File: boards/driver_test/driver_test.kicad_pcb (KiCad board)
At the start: 4 copper layers, 202.2 x 119.9 mm, 212 parts, among them J1 DIN41612_03x32_C, J2 Barrel_Jack_Switch, J3 Conn_01x24, J4 Conn_01x24, Q1 MMBT2222, Q10 MMBT2907, Q11 MMBT2222, Q12 MMBT2222, Q13 MMBT2222, Q14 MMBT2222, Q15 MMBT2222, Q16 MMBT2907, Q17 MMBT2222, Q18 MMBT2222, Q19 MMBT2222, Q2 MMBT2907, Q20 MMBT2222, Q21 MMBT2222, Q22 MMBT2222, Q23 MMBT2222, Q24 MMBT2222, Q25 MMBT2907, Q26 MMBT2222, Q27 MMBT2907, Q3 MMBT2222, Q4 IRF7413, Q5 MMBT2222, Q6 MMBT2907, Q7 MMBT2222, Q8 MMBT2222, Q9 MMBT2222, T1 1:1, T2 1:1, U1 AD1582BRTZ, U2 74LVC245, U3 JTE0624D05, U4 ADP151-3.3, U5 LTC4231-1, U6 74HC4514, U7 74LVC2G04, U8 SN7524

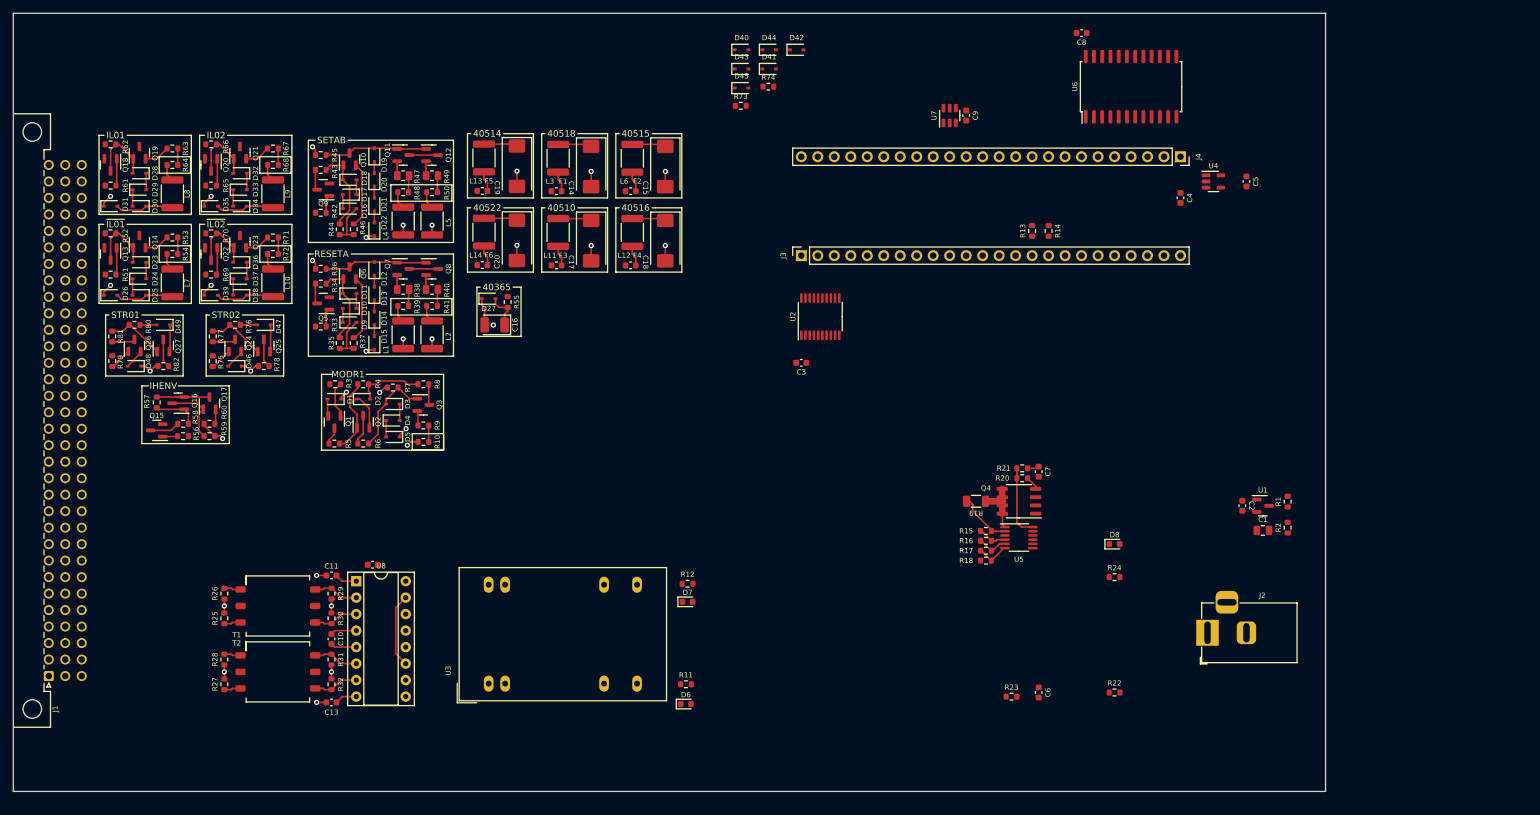
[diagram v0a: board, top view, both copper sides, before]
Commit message: Driver: some high-level board rearrangement and addition of 3d models
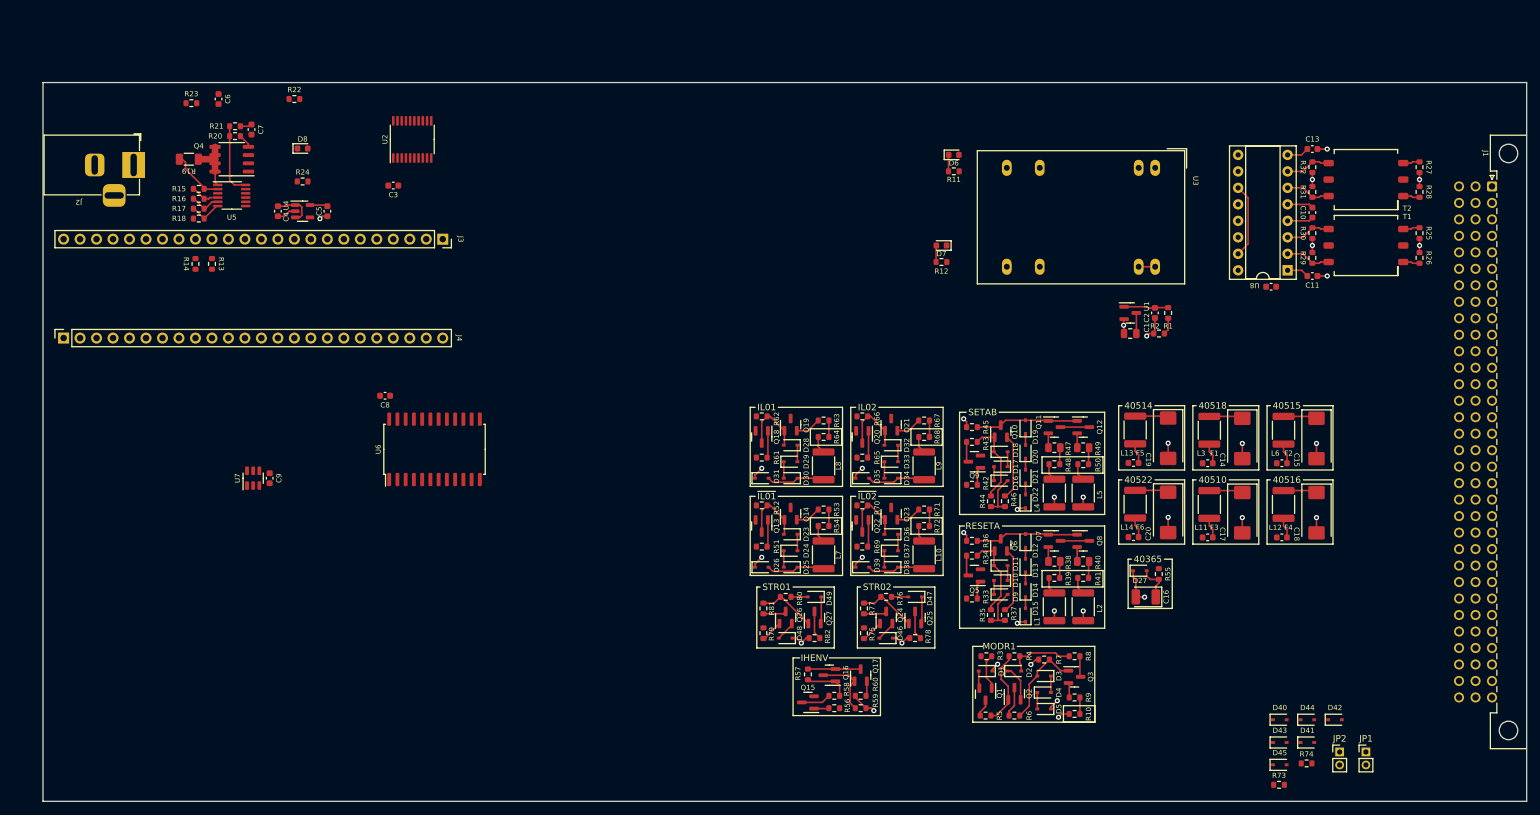
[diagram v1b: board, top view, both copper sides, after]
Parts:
- added JP1: Jumper_2_Open, Connector_PinHeader_2.00mm:PinHeader_1x02_P2.00mm_Vertical, F.Cu at (229.2, 128.5)
- added JP2: Jumper_2_Open, Connector_PinHeader_2.00mm:PinHeader_1x02_P2.00mm_Vertical, F.Cu at (225.2, 128.5)
- moved J1 234.8 mm to (248.7, 41.4), turned to -90 degrees
- moved R27 200.6 mm to (237.5, 38.4), turned to -90 degrees
- moved R28 197.7 mm to (237.5, 42.3), turned to -90 degrees
- moved R25 193.5 mm to (237.5, 48.6), turned to -90 degrees
- moved R26 191.3 mm to (237.5, 52.4), turned to -90 degrees
- moved T2 184.0 mm to (229.2, 40.3), turned to 180 degrees
- moved J2 180.5 mm to (39.4, 38.1), turned to 0 degrees
- moved T1 176.6 mm to (229.2, 50.5), turned to 180 degrees
- moved J4 174.3 mm to (28.6, 64.8), turned to 90 degrees
- moved C13 173.5 mm to (221.0, 35.6), turned to 180 degrees
- moved R32 170.8 mm to (221.0, 38.4), turned to 90 degrees
- moved R31 167.4 mm to (221.0, 42.3), turned to 90 degrees
- moved C10 164.8 mm to (221.0, 45.4), turned to 90 degrees
- moved R30 162.4 mm to (221.0, 48.6), turned to 90 degrees
- moved R29 159.7 mm to (221.0, 52.4), turned to 90 degrees
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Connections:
- net /40311/0V renamed /40311/4036nA
- J1 pad a1: /GAR1 -> unconnected-(J1-Pada1)
- J1 pad a10: /STR2 -> unconnected-(J1-Pada10)
- J1 pad a16: /RFD1 -> unconnected-(J1-Pada16)
- J1 pad a17: /XFN1 -> unconnected-(J1-Pada17)
- J1 pad a18: /RCD1 -> unconnected-(J1-Pada18)
- J1 pad a19: /XCN1 -> unconnected-(J1-Pada19)
- J1 pad a2: /GBR1 -> unconnected-(J1-Pada2)
- J1 pad a20: /RFD2 -> unconnected-(J1-Pada20)
- J1 pad a21: /XFN2 -> unconnected-(J1-Pada21)
- J1 pad a22: /RCD2 -> unconnected-(J1-Pada22)
- J1 pad a23: /XCN2 -> unconnected-(J1-Pada23)
- J1 pad a29: /XRST1 -> unconnected-(J1-Pada29)
- J1 pad a3: /GAR2 -> unconnected-(J1-Pada3)
- J1 pad a30: /RSTRN1 -> unconnected-(J1-Pada30)
- J1 pad a31: /XSET1 -> unconnected-(J1-Pada31)
- J1 pad a32: /SETRN1 -> unconnected-(J1-Pada32)
- J1 pad a4: /GBR2 -> unconnected-(J1-Pada4)
- J1 pad a9: /STR1 -> unconnected-(J1-Pada9)
- J1 pad c1: unconnected-(J1-Padc1) -> /GAR2
- J1 pad c10: unconnected-(J1-Padc10) -> /STR2
- J1 pad c16: unconnected-(J1-Padc16) -> /RFD1
- J1 pad c17: unconnected-(J1-Padc17) -> /XFN1
- J1 pad c18: unconnected-(J1-Padc18) -> /RCD1
- J1 pad c19: unconnected-(J1-Padc19) -> /XCN1
- J1 pad c2: unconnected-(J1-Padc2) -> /GBR2
- J1 pad c20: unconnected-(J1-Padc20) -> /RFD2
- J1 pad c21: unconnected-(J1-Padc21) -> /XFN2
- J1 pad c22: unconnected-(J1-Padc22) -> /RCD2
- J1 pad c23: unconnected-(J1-Padc23) -> /XCN2
- J1 pad c29: unconnected-(J1-Padc29) -> /XRST1
- J1 pad c3: unconnected-(J1-Padc3) -> /GAR1
- J1 pad c30: unconnected-(J1-Padc30) -> /RSTRN1
- J1 pad c31: unconnected-(J1-Padc31) -> /XSET1
- J1 pad c32: unconnected-(J1-Padc32) -> /SETRN1
- J1 pad c4: unconnected-(J1-Padc4) -> /GBR1
- J1 pad c9: unconnected-(J1-Padc9) -> /STR1
- R73 pad 1: /XRST1 -> Net-(JP1-Pad2)
- R74 pad 1: /XSET1 -> Net-(JP2-Pad2)
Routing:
- net GND: track 67.3 -> 77.6 mm, vias 30 -> 33
- net Net-(C2-Pad1): track 0.00 -> 6.88 mm
- net Net-(C4-Pad2): track 0.00 -> 6.30 mm
- net +5V: track 0.00 -> 3.18 mm
- net +3V3: track 0.00 -> 2.74 mm
- net /VREF: track 4.02 -> 6.61 mm
- net Net-(D7-Pad2): track 0.00 -> 2.56 mm
- net Net-(D6-Pad1): track 0.00 -> 2.56 mm
- net Net-(J2-Pad1): track 8.53 -> 11.1 mm
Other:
- board size 202.2 x 119.9 mm -> 228.6 x 110.7 mm

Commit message: Driver test: completed much of the preliminary layout.
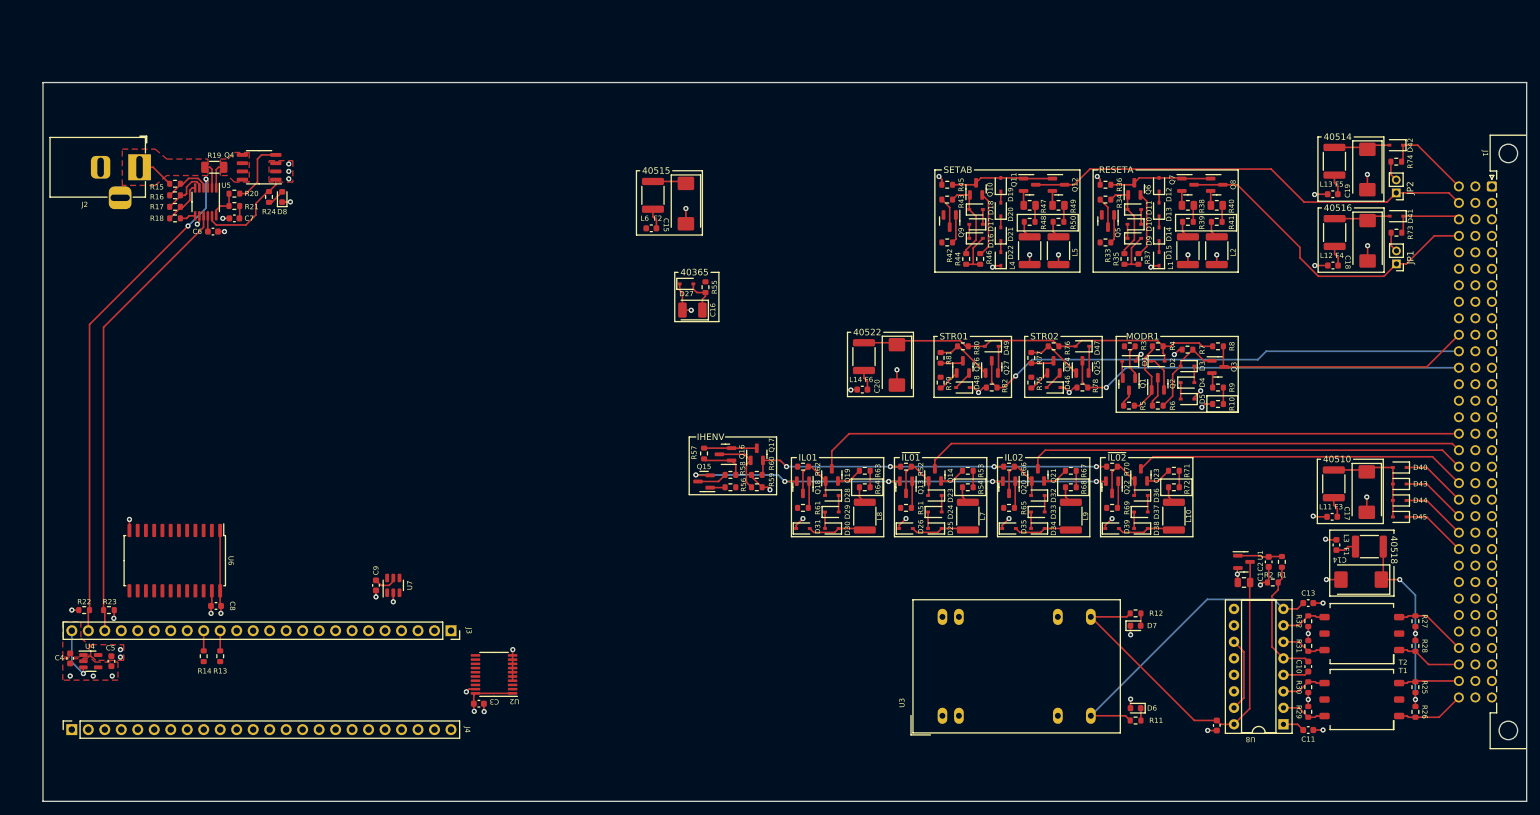
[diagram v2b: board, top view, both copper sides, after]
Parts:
- moved C15 103.7 mm to (124.5, 44.0)
- moved F2 103.7 mm to (119.1, 47.9)
- moved L6 103.7 mm to (119.4, 42.8)
- moved R74 93.7 mm to (233.9, 37.6)
- moved U3 90.6 mm to (164.0, 123.0), turned to 90 degrees
- moved D6 89.7 mm to (193.7, 121.8), turned to 180 degrees
- moved R11 89.1 mm to (193.7, 123.7), turned to 0 degrees
- moved D42 89.0 mm to (233.9, 35.1), turned to 180 degrees
- moved R73 87.0 mm to (233.9, 48.5)
- moved JP2 86.6 mm to (233.9, 42.4), turned to 180 degrees
- moved R22 85.1 mm to (31.8, 106.7), turned to 180 degrees
- moved U2 83.4 mm to (94.9, 116.6), turned to 180 degrees
- moved C16 82.7 mm to (125.5, 60.5)
- moved D27 82.7 mm to (124.6, 56.4)
- moved R55 82.7 mm to (127.5, 56.9)
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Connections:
- net Net-(C4-Pad2) renamed /FPGA and Power/5V_FPGA
- J1 pad c1: /GAR2 -> /SETRN1
- J1 pad c10: /STR2 -> /MODR1
- J1 pad c11: unconnected-(J1-Padc11) -> /STR1
- J1 pad c12: unconnected-(J1-Padc12) -> /STR2
- J1 pad c16: /RFD1 -> /XFN1
- J1 pad c17: /XFN1 -> /XCN1
- J1 pad c18: /RCD1 -> /XFN2
- J1 pad c19: /XCN1 -> /XCN2
- J1 pad c2: /GBR2 -> /XSET1
- J1 pad c20: /RFD2 -> /RFD1
- J1 pad c21: /XFN2 -> /RCD1
- J1 pad c22: /RCD2 -> /RFD2
- J1 pad c23: /XCN2 -> /RCD2
- J1 pad c29: /XRST1 -> /GAR2
- J1 pad c3: /GAR1 -> /RSTRN1
- J1 pad c30: /RSTRN1 -> /GBR2
- J1 pad c31: /XSET1 -> /GAR1
- J1 pad c32: /SETRN1 -> /GBR1
- J1 pad c4: /GBR1 -> /XRST1
- J1 pad c9: /STR1 -> unconnected-(J1-Padc9)
- J2 pad 1: Net-(J2-Pad1) -> /FPGA and Power/14V_IN
- J3 pad 22: unconnected-(J3-Pad22) -> /FPGA and Power/PG_14V
- J3 pad 23: unconnected-(J3-Pad23) -> /FPGA and Power/EN_14V
- J4 pad 23: /FPGA and Power/PG_14V -> unconnected-(J4-Pad23)
- J4 pad 24: /FPGA and Power/EN_14V -> unconnected-(J4-Pad24)
- Q4 pad 5: Net-(Q4-Pad5) -> /FPGA and Power/14V_SENSE
- Q4 pad 6: Net-(Q4-Pad5) -> /FPGA and Power/14V_SENSE
- Q4 pad 7: Net-(Q4-Pad5) -> /FPGA and Power/14V_SENSE
- Q4 pad 8: Net-(Q4-Pad5) -> /FPGA and Power/14V_SENSE
- R13 pad 2: Net-(J2-Pad1) -> /FPGA and Power/14V_IN
- R15 pad 2: Net-(J2-Pad1) -> /FPGA and Power/14V_IN
- R19 pad 1: Net-(Q4-Pad5) -> /FPGA and Power/14V_IN
- R19 pad 2: Net-(J2-Pad1) -> /FPGA and Power/14V_SENSE
- U3 pad 22: Net-(J2-Pad1) -> /FPGA and Power/14V_IN
- U3 pad 23: Net-(J2-Pad1) -> /FPGA and Power/14V_IN
- U5 pad 1: Net-(Q4-Pad5) -> /FPGA and Power/14V_SENSE
- U5 pad 2: Net-(J2-Pad1) -> /FPGA and Power/14V_IN
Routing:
- net /XFN1: track 0.00 -> 100.5 mm
- net /XCN1: track 0.00 -> 83.6 mm
- net /FPGA and Power/EN_14V: track 0.00 -> 78.5 mm, vias 0 -> 2
- net /STR1: track 4.45 -> 77.9 mm, vias 0 -> 1
- net /40311/4036nA: track 5.79 -> 76.9 mm, vias 0 -> 5
- net /FPGA and Power/PG_14V: track 0.00 -> 70.4 mm
- net /XFN2: track 0.00 -> 68.1 mm
- net /XSET1: track 4.44 -> 69.5 mm
- net /STR2: track 4.45 -> 62.9 mm, vias 0 -> 1
- net +5V: track 3.18 -> 61.3 mm
- net /40331A: track 2.29 -> 58.7 mm, vias 0 -> 4
- net /XCN2: track 0.00 -> 51.4 mm
- net /XRST1: track 4.44 -> 50.2 mm
- net -5V: track 3.42 -> 47.5 mm
- net /MODR1: track 3.22 -> 41.5 mm
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- added copper zone on F.Cu, net +14V
- added copper zone on In2.Cu, net +14V
- added copper zone on F.Cu, net +3V3
- added copper zone on In2.Cu, net +3V3
- added copper zone on F.Cu, net /FPGA and Power/14V_IN
- added copper zone on F.Cu, net /FPGA and Power/14V_SENSE
- added copper zone on F.Cu, net /FPGA and Power/5V_FPGA
- added copper zone on F.Cu, net GND

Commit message: Driver test: finished up board layout
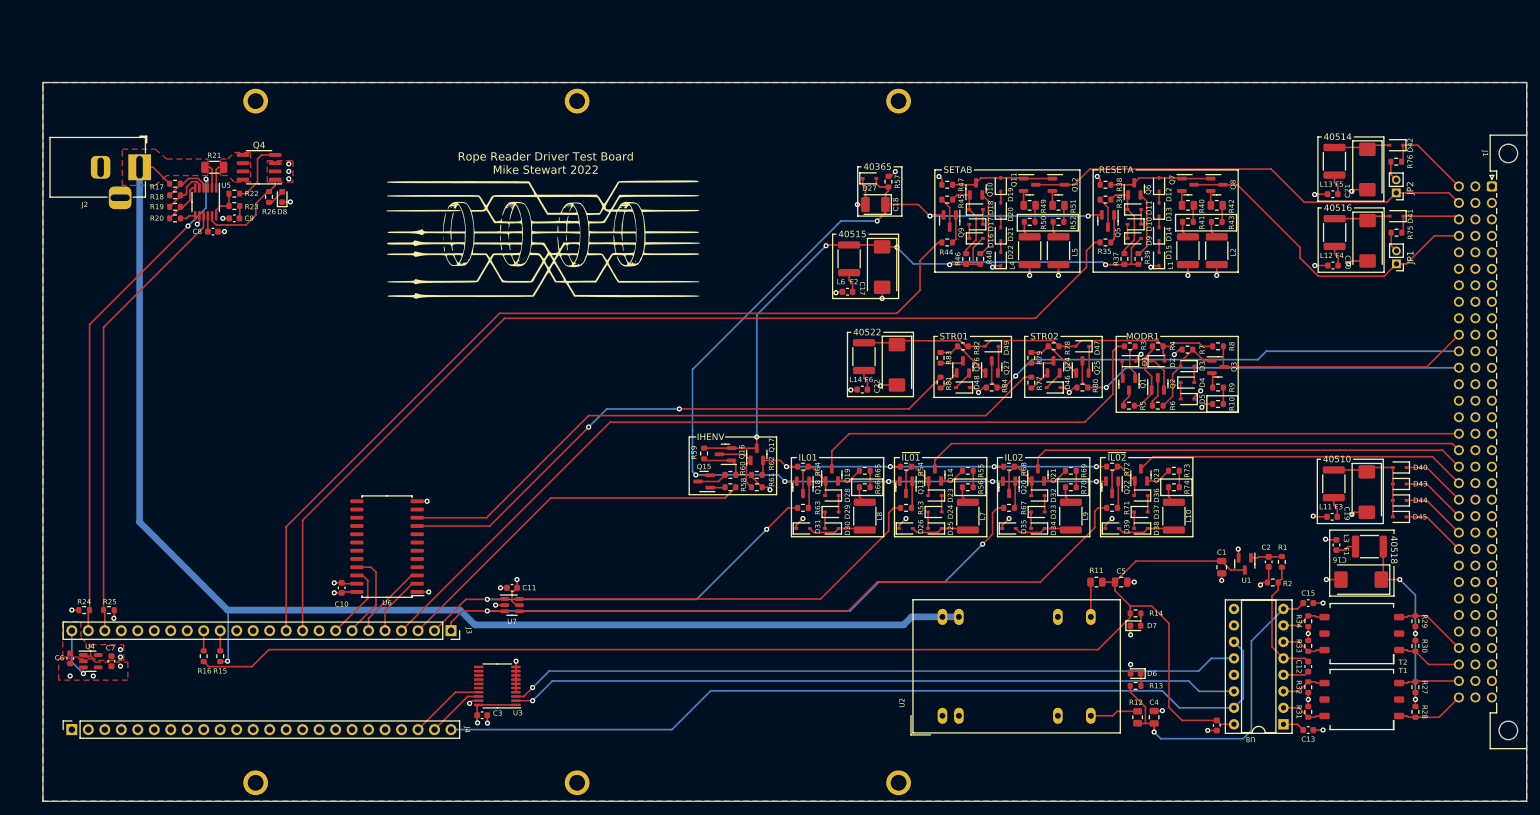
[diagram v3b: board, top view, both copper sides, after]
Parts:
- added C4: 1.0uF, Capacitor_SMD:C_0805_2012Metric, F.Cu at (196.6, 123.2)
- added C5: 1.0uF, Capacitor_SMD:C_0805_2012Metric, F.Cu at (191.5, 102.4)
- added G***: LOGO, lachesis:cores, F.Cu at (102.1, 49.3)
- added H1: MountingHole_Pad, lachesis:MountingHole_No2_Pad, F.Cu at (58.2, 28.3)
- added H2: MountingHole_Pad, lachesis:MountingHole_No2_Pad, F.Cu at (107.7, 28.3)
- added H3: MountingHole_Pad, lachesis:MountingHole_No2_Pad, F.Cu at (58.2, 133.3)
- added H4: MountingHole_Pad, lachesis:MountingHole_No2_Pad, F.Cu at (157.2, 28.3)
- added H5: MountingHole_Pad, lachesis:MountingHole_No2_Pad, F.Cu at (107.7, 133.3)
- added H6: MountingHole_Pad, lachesis:MountingHole_No2_Pad, F.Cu at (157.2, 133.3)
- added R11: 0, Resistor_SMD:R_0805_2012Metric, F.Cu at (187.7, 102.4)
- added R12: 0, Resistor_SMD:R_0805_2012Metric, F.Cu at (194.1, 123.2)
- Q4: footprint Package_SO:SO-8_3.9x4.9mm_P1.27mm -> Package_SO:SOIC-8_3.9x4.9mm_P1.27mm
- moved U6 32.8 mm to (78.4, 96.9), turned to 180 degrees
- moved R57 32.5 mm to (155.7, 40.7)
- moved C18 32.5 mm to (153.7, 44.2)
- moved D27 32.5 mm to (152.7, 40.2)
- moved C17 31.8 mm to (154.7, 53.8)
- moved F2 31.8 mm to (149.4, 57.6)
- moved L6 31.8 mm to (149.6, 52.6)
- moved C11 21.0 mm to (97.7, 103.3), turned to 180 degrees
- moved C10 19.6 mm to (71.4, 103.3), turned to -90 degrees
- moved U7 18.5 mm to (97.7, 105.9), turned to 0 degrees
- moved D6 5.33 mm to (193.7, 116.5)
- moved R13 5.33 mm to (193.7, 118.4)
- moved C1 4.16 mm to (207.0, 100.1), turned to 90 degrees
- moved U3 1.85 mm to (95.4, 118.4)
- moved C3 1.85 mm to (93.1, 122.9)
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- renumbered C8 to C10, C9 to C11, C10 to C12, C11 to C13, C12 to C14, C13 to C15, C14 to C16, C15 to C17, C16 to C18, C17 to C19, C18 to C20, C19 to C21, C20 to C22, C4 to C6, C5 to C7, C6 to C8, C7 to C9, R11 to R13, R12 to R14, R13 to R15, R14 to R16, R15 to R17, R16 to R18, R17 to R19, R18 to R20, R19 to R21, R20 to R22, R21 to R23, R22 to R24, R23 to R25, R24 to R26, R25 to R27, R26 to R28, R27 to R29, R28 to R30, R29 to R31, R30 to R32, R31 to R33, R32 to R34, R33 to R35, R34 to R36, R35 to R37, R36 to R38, R37 to R39, R38 to R40, R39 to R41, R40 to R42, R41 to R43, R42 to R44, R43 to R45, R44 to R46, R45 to R47, R46 to R48, R47 to R49, R48 to R50, R49 to R51, R50 to R52, R51 to R53, R52 to R54, R53 to R55, R54 to R56, R55 to R57, R56 to R58, R57 to R59, R58 to R60, R59 to R61, R60 to R62, R61 to R63, R62 to R64, R63 to R65, R64 to R66, R65 to R67, R66 to R68, R67 to R69, R68 to R70, R69 to R71, R70 to R72, R71 to R73, R72 to R74, R73 to R75, R74 to R76, R75 to R77, R76 to R78, R77 to R79, R78 to R80, R79 to R81, R80 to R82, R81 to R83, R82 to R84, U3 to U2, U2 to U3
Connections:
- J3 pad 1: /FPGA and Power/SAF1 -> /FPGA and Power/IL2
- J3 pad 10: unconnected-(J3-Pad10) -> /FPGA and Power/RESET1
- J3 pad 11: unconnected-(J3-Pad11) -> /FPGA and Power/SET1
- J3 pad 19: /FPGA and Power/SBF -> unconnected-(J3-Pad19)
- J3 pad 2: /FPGA and Power/SAF2 -> /FPGA and Power/IL1
- J3 pad 3: unconnected-(J3-Pad3) -> /40331/IN
- J3 pad 4: unconnected-(J3-Pad4) -> /FPGA and Power/ROPER
- J3 pad 5: unconnected-(J3-Pad5) -> /FPGA and Power/STRA0
- J3 pad 6: unconnected-(J3-Pad6) -> /FPGA and Power/STRA1
- J3 pad 7: unconnected-(J3-Pad7) -> /FPGA and Power/STRA2
- J3 pad 8: unconnected-(J3-Pad8) -> /FPGA and Power/STRA3
- J4 pad 14: /FPGA and Power/IL2 -> unconnected-(J4-Pad14)
- J4 pad 15: /FPGA and Power/IL1 -> unconnected-(J4-Pad15)
- J4 pad 19: /FPGA and Power/RESET1 -> unconnected-(J4-Pad19)
- J4 pad 21: /FPGA and Power/SET1 -> unconnected-(J4-Pad21)
- J4 pad 22: /FPGA and Power/ROPER -> /FPGA and Power/SAF2
- J4 pad 23: unconnected-(J4-Pad23) -> /FPGA and Power/SAF1
- J4 pad 24: unconnected-(J4-Pad24) -> /FPGA and Power/SBF
- J4 pad 3: /FPGA and Power/STRA3 -> unconnected-(J4-Pad3)
- J4 pad 4: /FPGA and Power/STRA2 -> unconnected-(J4-Pad4)
- J4 pad 5: /FPGA and Power/STRA1 -> unconnected-(J4-Pad5)
- J4 pad 6: /FPGA and Power/STRA0 -> unconnected-(J4-Pad6)
- J4 pad 7: /40331/IN -> unconnected-(J4-Pad7)
- U2 pad 11: -5V -> Net-(R12-Pad2)
- U2 pad 14: +5V -> Net-(R11-Pad2)
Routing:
- net /FPGA and Power/14V_IN: track 9.80 -> 206.9 mm, vias 0 -> 1
- net /FPGA and Power/RESET1: track 0.00 -> 159.1 mm
- net +5V: track 61.3 -> 207.6 mm
- net /FPGA and Power/SET1: track 0.00 -> 137.9 mm
- net /FPGA and Power/ROPER: track 0.00 -> 133.4 mm
- net /FPGA and Power/SBF: track 11.4 -> 135.5 mm
- net /FPGA and Power/SA2: track 0.00 -> 113.1 mm, vias 0 -> 1
- net /FPGA and Power/SA1: track 0.00 -> 112.6 mm, vias 0 -> 1
- net /40601b/SEn: track 0.00 -> 103.6 mm
- net /40314/IN: track 0.00 -> 98.6 mm
- net /FPGA and Power/IL2: track 0.00 -> 98.4 mm, vias 0 -> 2
- net /40311/4036nA: track 76.9 -> 170.6 mm, vias 5 -> 8
- net /40601a/SEn: track 0.00 -> 90.1 mm, vias 0 -> 2
- net /BPLIZ1: track 26.9 -> 107.5 mm, vias 0 -> 5
- net /FPGA and Power/IL1: track 0.00 -> 66.5 mm, vias 0 -> 2
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- added copper zone on B.Cu, net GND
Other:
- board text added: "Rope Reader Driver Test Board Mike Stewart 2022"
